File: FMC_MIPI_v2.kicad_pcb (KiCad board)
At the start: 6 copper layers, 69 x 112 mm, 59 parts, among them J1 ASP-134488-01, J2 QTH-060-01-L-D-A, U2 SN74AVC2T45DCUR, U5 TS3DDR3812_RUA_42, U6 TS3DDR3812_RUA_42, U8 SN74AVCH16T245_DGV_48

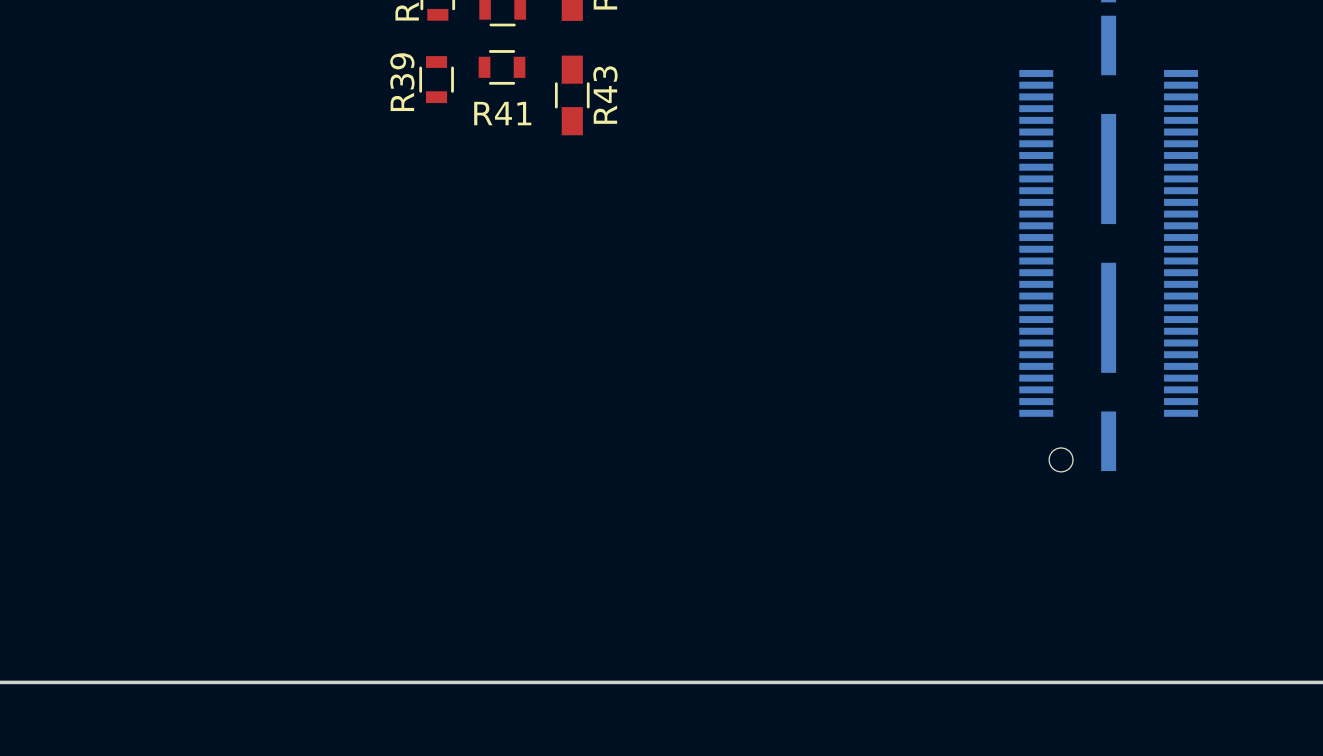
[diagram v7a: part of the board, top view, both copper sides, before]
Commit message: added EEPROM
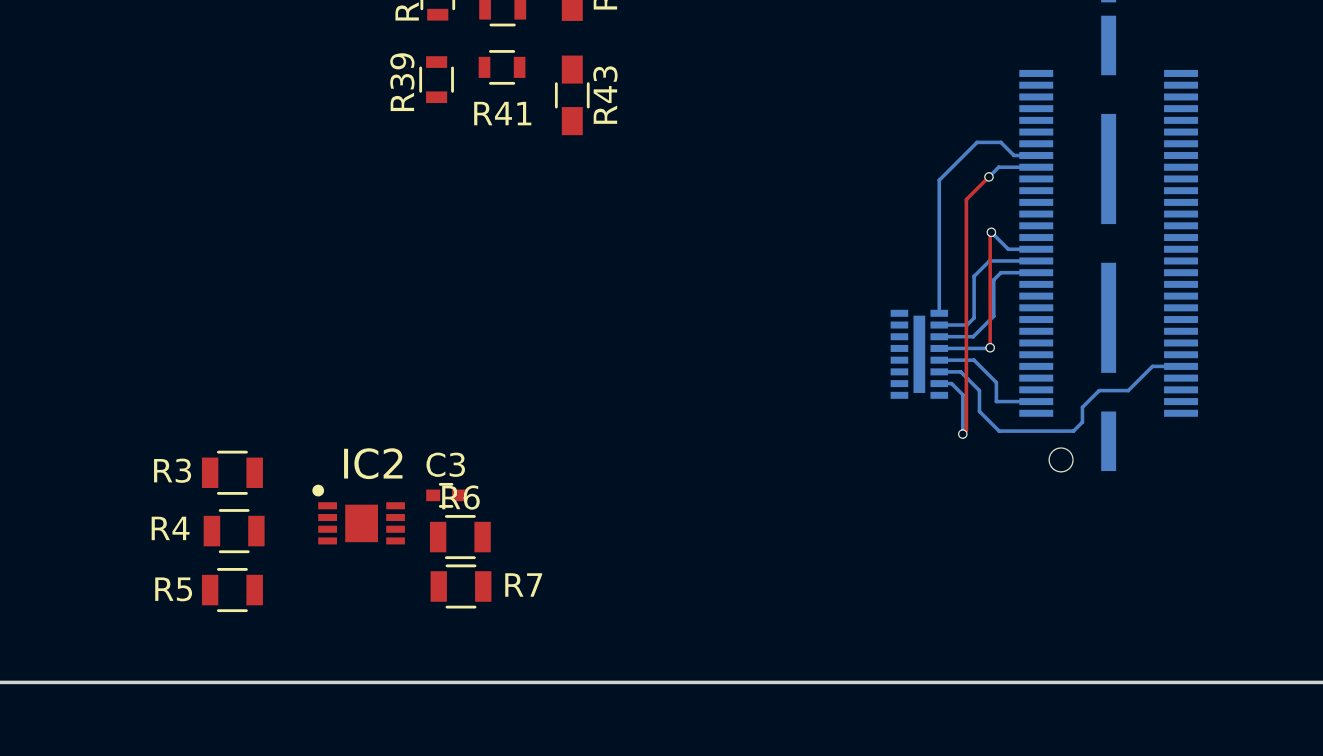
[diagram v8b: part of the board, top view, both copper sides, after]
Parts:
- added C3: 0.1uF, Capacitors_SMD:C_0402, F.Cu at (121.6, 133.0)
- added IC1: ECLAMP2398P.TCT, SON50P160X400X65-17N, B.Cu at (141.8, 127.0)
- added IC2: AT24MAC402-MAHM-T, SON50P300X200X60-9N, F.Cu at (118.0, 134.2)
- added R3: 4.7k, Resistors_SMD:R_0805, F.Cu at (112.5, 132.1)
- added R4: 4.7k, Resistors_SMD:R_0805, F.Cu at (112.5, 134.5)
- added R5: 4.7k, Resistors_SMD:R_0805, F.Cu at (112.5, 137.1)
- added R6: 0, Resistors_SMD:R_0805, F.Cu at (122.2, 134.8)
- added R7: 0, Resistors_SMD:R_0805, F.Cu at (122.2, 136.9)
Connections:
- J1 pad E1: (no net) -> Earth
- J1 pad E11: (no net) -> Earth
- J1 pad E14: (no net) -> Earth
- J1 pad E17: (no net) -> Earth
- J1 pad E20: (no net) -> Earth
- J1 pad E23: (no net) -> Earth
- J1 pad E26: (no net) -> Earth
- J1 pad E29: (no net) -> Earth
- J1 pad E32: (no net) -> Earth
- J1 pad E35: (no net) -> Earth
- J1 pad E38: (no net) -> Earth
- J1 pad E40: (no net) -> Earth
- J1 pad E5: (no net) -> Earth
- J1 pad E8: (no net) -> Earth
- J1 pad F12: (no net) -> Earth
- J1 pad F15: (no net) -> Earth
- J1 pad F18: (no net) -> Earth
- J1 pad F2: (no net) -> Earth
- J1 pad F21: (no net) -> Earth
- J1 pad F24: (no net) -> Earth
- J1 pad F27: (no net) -> Earth
- J1 pad F3: (no net) -> Earth
- J1 pad F30: (no net) -> Earth
- J1 pad F33: (no net) -> Earth
- J1 pad F36: (no net) -> Earth
- J1 pad F39: (no net) -> Earth
- J1 pad F6: (no net) -> Earth
- J1 pad F9: (no net) -> Earth
- J1 pad G1: (no net) -> Earth
- J1 pad G11: (no net) -> Earth
- J1 pad G14: (no net) -> Earth
- J1 pad G17: (no net) -> Earth
- J1 pad G20: (no net) -> Earth
- J1 pad G23: (no net) -> Earth
- J1 pad G26: (no net) -> Earth
- J1 pad G29: (no net) -> Earth
- J1 pad G32: (no net) -> Earth
- J1 pad G35: (no net) -> Earth
- J1 pad G38: (no net) -> Earth
- J1 pad G4: (no net) -> Earth
- J1 pad G40: (no net) -> Earth
- J1 pad G5: (no net) -> Earth
- J1 pad G8: (no net) -> Earth
- J1 pad H12: (no net) -> Earth
- J1 pad H15: (no net) -> Earth
- J1 pad H18: (no net) -> Earth
- J1 pad H21: (no net) -> Earth
- J1 pad H24: (no net) -> Earth
- J1 pad H27: (no net) -> Earth
- J1 pad H3: (no net) -> Earth
- J1 pad H30: (no net) -> Earth
- J1 pad H33: (no net) -> Earth
- J1 pad H36: (no net) -> Earth
- J1 pad H39: (no net) -> Earth
- J1 pad H6: (no net) -> Earth
- J1 pad H9: (no net) -> Earth
- J1 pad J1: (no net) -> Earth
- J1 pad J11: (no net) -> Earth
- J1 pad J14: (no net) -> Earth
- J1 pad J17: (no net) -> Earth
- J1 pad J20: (no net) -> Earth
- J1 pad J23: (no net) -> Earth
- J1 pad J26: (no net) -> Earth
- J1 pad J29: (no net) -> Earth
- J1 pad J32: (no net) -> Earth
- J1 pad J35: (no net) -> Earth
- J1 pad J38: (no net) -> Earth
- J1 pad J4: (no net) -> Earth
- J1 pad J40: (no net) -> Earth
- J1 pad J5: (no net) -> Earth
- J1 pad J8: (no net) -> Earth
- J1 pad K12: (no net) -> Earth
- J1 pad K15: (no net) -> Earth
- J1 pad K18: (no net) -> Earth
- J1 pad K2: (no net) -> Earth
- J1 pad K21: (no net) -> Earth
- J1 pad K24: (no net) -> Earth
- J1 pad K27: (no net) -> Earth
- J1 pad K3: (no net) -> Earth
- J1 pad K30: (no net) -> Earth
- J1 pad K33: (no net) -> Earth
- J1 pad K36: (no net) -> Earth
- J1 pad K39: (no net) -> Earth
- J1 pad K6: (no net) -> Earth
- J1 pad K9: (no net) -> Earth
- J2 pad 112: (no net) -> /Jetson_connector/JT_1p8V_GPIO9_IN
- J2 pad 117: (no net) -> /Jetson_connector/JT_1p8V_GPIO17_IN
- J2 pad 75: (no net) -> /Jetson_connector/JT_1p8V_I2C_CAM_CLK
- J2 pad 77: (no net) -> /Jetson_connector/JT_1p8V_I2C_CAM_DAT
- J2 pad 91: (no net) -> /Jetson_connector/JT_1p8V_CAM0_MCLK
- J2 pad 93: (no net) -> /Jetson_connector/JT_1p8V_CAM0_PWR
- J2 pad 95: (no net) -> /Jetson_connector/JT_1p8V_CAM0_RST
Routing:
- net /Jetson_connector/JT_1p8V_I2C_CAM_DAT: track 0.00 -> 16.5 mm, vias 0 -> 2
- net /Jetson_connector/JT_1p8V_GPIO9_IN: track 0.00 -> 13.4 mm
- net /Jetson_connector/JT_1p8V_I2C_CAM_CLK: track 0.00 -> 10.9 mm
- net /Jetson_connector/JT_1p8V_CAM0_MCLK: track 0.00 -> 9.35 mm, vias 0 -> 2
- net /Jetson_connector/JT_1p8V_CAM0_PWR: track 0.00 -> 6.31 mm
- net /Jetson_connector/JT_1p8V_CAM0_RST: track 0.00 -> 6.18 mm
- net /Jetson_connector/JT_1p8V_GPIO17_IN: track 0.00 -> 5.35 mm
